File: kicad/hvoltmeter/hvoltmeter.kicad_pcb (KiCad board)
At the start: 2 copper layers, 14.4 x 24.9 mm, 34 parts, among them J1 USB_B_Micro-Connector, J2 SWC, J3 SWD, J4 Conn, J5 Conn, J6 Conn, SW1 SW_DPDT_x2, U1 LTC4054ES5-4.2, U2 AD8541, U3 MCP1700

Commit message: удалено:       STM32Cube/HV/.cproject 	удалено:       STM32Cube/HV/.mxproject 	удалено:       STM32Cube/HV/.project 	удалено:       STM32Cube/HV/.settings/language.settings.xml 	удалено:       STM32Cube/HV/.settings/stm32cubeide.project.prefs 	удалено:       STM32Cube/HV/Core/Inc/main.h 	удалено:       STM32Cube/HV/Core/Inc/stm32g0xx_hal_conf.h 	удалено:       STM32Cube/HV/Core/Inc/stm32g0xx_it.h 	удалено:       STM32Cube/HV/Core/Src/main.c 	удалено:       STM32Cube/HV/Core/Src/stm32g0xx_hal_msp.c 	удалено:       STM32Cube/HV/Core/Src/stm32g0xx_it.c 	удалено:       STM32Cube/HV/Core/Src/syscalls.c 	удалено:       STM32Cube/HV/Core/Src/sysmem.c 	удалено:       STM32Cube/HV/Core/Src/system_stm32g0xx.c 	удалено:       STM32Cube/HV/Core/Startup/startup_stm32g031f8px.s 	удалено:       STM32Cube/HV/Drivers/CMSIS/Device/ST/STM32G0xx/Include/stm32g031xx.h 	удалено:       STM32Cube/HV/Drivers/CMSIS/Device/ST/STM32G0xx/Include/stm32g0xx.h 	удалено:       STM32Cube/HV/Drivers/CMSIS/Device/ST/STM32G0xx/Include/system_stm32g0xx.h 	удалено:       STM32Cube/HV/Drivers/CMSIS/Include/cmsis_armcc.h 	удалено:       STM32Cube/HV/Drivers/CMSIS/Include/cmsis_armclang.h 	удалено:       STM32Cube/HV/Drivers/CMSIS/Include/cmsis_armclang_ltm.h 	удалено:       STM32Cube/HV/Drivers/CMSIS/Include/cmsis_compiler.h 	удалено:       STM32Cube/HV/Drivers/CMSIS/Include/cmsis_gcc.h 	удалено:       STM32Cube/HV/Drivers/CMSIS/Include/cmsis_iccarm.h 	удалено:       STM32Cube/HV/Drivers/CMSIS/Include/cmsis_version.h 	удалено:       STM32Cube/HV/Drivers/CMSIS/Include/core_armv81mml.h 	удалено:       STM32Cube/HV/Drivers/CMSIS/Include/core_armv8mbl.h 	удалено:       STM32Cube/HV/Drivers/CMSIS/Include/core_armv8mml.h 	удалено:       STM32Cube/HV/Drivers/CMSIS/Include/core_cm0.h 	удалено:       STM32Cube/HV/Drivers/CMSIS/Include/core_cm0plus.h 	удалено:       STM32Cube/HV/Drivers/CMSIS/Include/core_cm1.h 	удалено:       STM32Cube/HV/Drivers/CMSIS/Include/core_cm23.h 	удалено:       STM32Cube/HV/Drivers/CMSIS/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
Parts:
- R6: value 10G -> 5G
- R8: value 4.7k -> 10k
- moved C11 30.4 mm to (38.5, 63.5)
- moved C12 27.9 mm to (40.6, 63.5)
- moved C9 26.3 mm to (41.7, 63.5), turned to 270 degrees
- moved R3 26.3 mm to (47.5, 68.8), turned to 90 degrees
- moved R4 25.8 mm to (39.5, 66.3)
- moved C1 25.5 mm to (40.0, 75.4)
- moved C2 25.5 mm to (42.2, 68.2)
- moved C5 25.5 mm to (47.7, 65.2)
- moved R5 25.5 mm to (48.0, 76.4)
- moved C3 25.5 mm to (40.1, 61.5)
- moved C4 25.5 mm to (46.7, 73.2)
- moved C6 25.5 mm to (47.5, 68.8)
- moved C7 25.5 mm to (46.7, 76.5)
- moved D1 25.5 mm to (41.6, 62.5)
- moved J4 25.5 mm to (38.2, 59.8)
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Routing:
- net Net-(D2-Pad15): track 2.99 -> 10.7 mm
- net SDA: track 15.9 -> 9.25 mm
- net +BATT: track 21.7 -> 16.2 mm
- net Net-(D3-Pad12): track 1.84 -> 4.34 mm
- net SCL: track 7.03 -> 9.30 mm
- net GND: track 65.3 -> 66.8 mm
- net Net-(D3-Pad9): track 1.89 -> 3.32 mm
- net +2V8: track 42.3 -> 43.2 mm
- net Net-(D2-Pad18): track 4.77 -> 4.03 mm

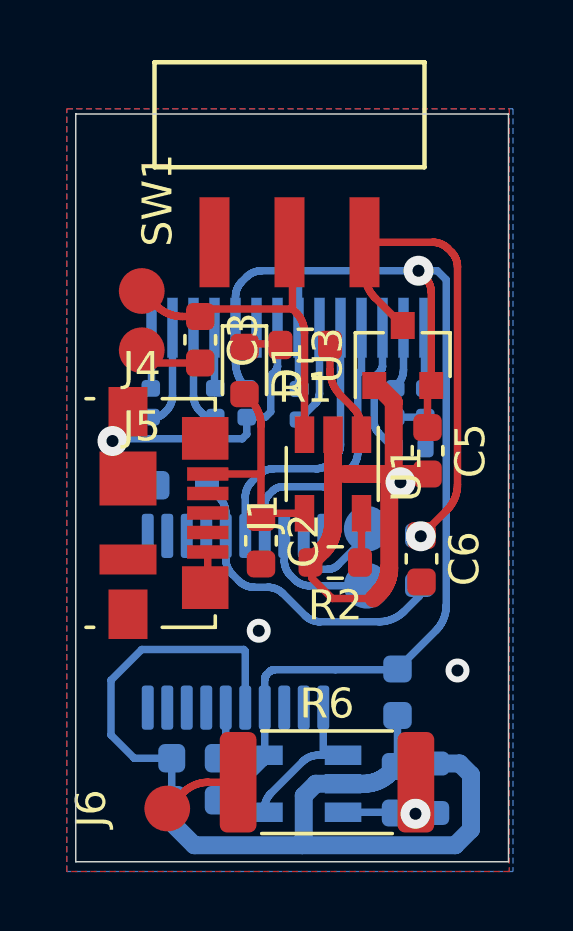
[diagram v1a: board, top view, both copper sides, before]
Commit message: изменено:      kicad/hvoltmeter/hvoltmeter.kicad_pcb 	изменено:      kicad/hvoltmeter/hvoltmeter.kicad_pcb-bak 	изменено:      kicad/hvoltmeter/hvoltmeter.sch 	изменено:      kicad/hvoltmeter/hvoltmeter.sch-bak
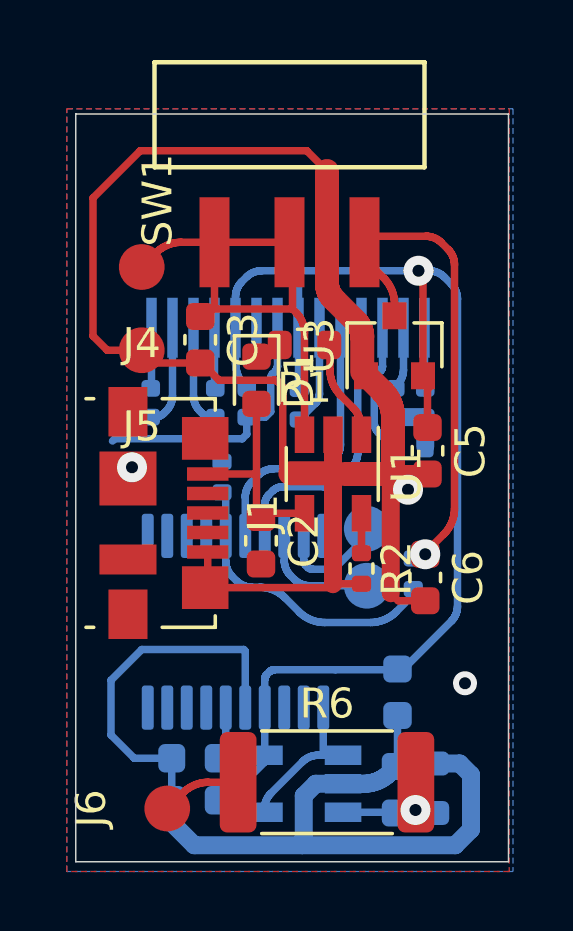
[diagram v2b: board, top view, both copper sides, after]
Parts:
- R2: footprint Resistor_SMD:R_0603_1608Metric -> Resistor_SMD:R_0402_1005Metric
- R3: value R -> 10k; footprint Resistor_SMD:R_0603_1608Metric -> Resistor_SMD:R_0402_1005Metric
- R4: value R -> 20k; footprint Resistor_SMD:R_0603_1608Metric -> Resistor_SMD:R_0402_1005Metric
- moved R4 1.35 mm to (40.9, 66.0), turned to 90 degrees
- moved R2 0.90 mm to (45.5, 69.1), turned to 270 degrees
- moved J4 0.80 mm to (38.2, 59.0)
- moved C6 0.64 mm to (47.6, 69.4)
- moved D1 0.52 mm to (42.0, 62.8)
- moved R3 0.49 mm to (47.2, 69.2)
- moved U3 0.43 mm to (46.6, 61.6)
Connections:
- SW1 pad 3: (no net) -> Net-(C3-Pad1)
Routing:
- net GND: track 66.8 -> 100.8 mm, vias 4 -> 3
- net Net-(C3-Pad1): track 12.0 -> 17.2 mm
- net Net-(D2-Pad15): track 10.7 -> 9.97 mm
- net Net-(C2-Pad1): track 7.58 -> 6.98 mm

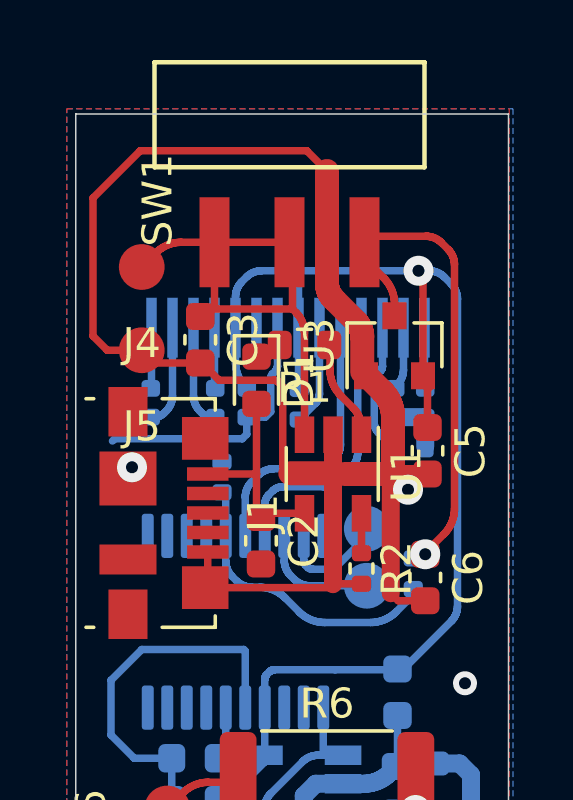
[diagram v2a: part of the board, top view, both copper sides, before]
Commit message: изменено:      kicad/hvoltmeter/hvoltmeter.kicad_pcb 	изменено:      kicad/hvoltmeter/hvoltmeter.kicad_pcb-bak 	изменено:      kicad/hvoltmeter/hvoltmeter.sch 	изменено:      kicad/hvoltmeter/hvoltmeter.sch-bak
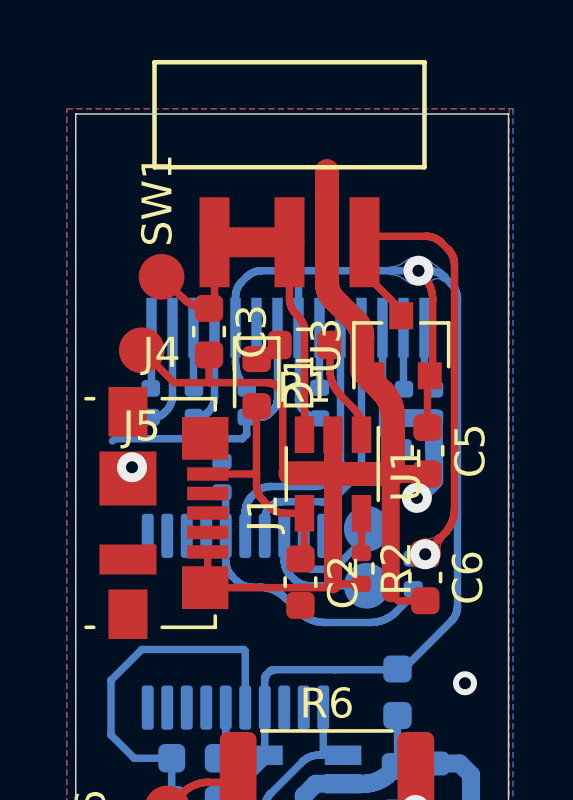
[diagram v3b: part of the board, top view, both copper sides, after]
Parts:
- moved C2 1.91 mm to (43.5, 69.5)
- moved J4 0.74 mm to (38.9, 59.4)
- moved C12 0.71 mm to (39.9, 63.5), turned to 270 degrees
- moved R8 0.68 mm to (44.1, 63.6), turned to 270 degrees
- moved C3 0.40 mm to (40.4, 61.2)
- moved C10 0.29 mm to (46.9, 63.6)
- moved C13 0.29 mm to (47.9, 63.6)
- moved R7 0.29 mm to (47.4, 65.1)
- moved U3 0.23 mm to (46.9, 61.6)
- moved D1 0.08 mm to (42.0, 62.9)
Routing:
- net GND: track 100.8 -> 88.3 mm
- net Net-(C3-Pad1): track 17.2 -> 13.3 mm
- net +2V8: track 43.2 -> 45.0 mm
- net Net-(C12-Pad1): track 3.41 -> 2.03 mm
- net Net-(C12-Pad2): track 2.03 -> 3.39 mm
- net Net-(D3-Pad9): track 3.32 -> 2.00 mm
- net Net-(C2-Pad1): track 6.98 -> 8.01 mm

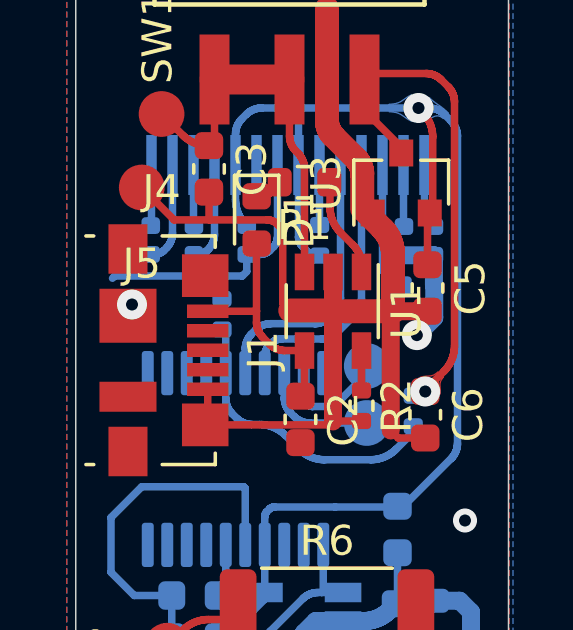
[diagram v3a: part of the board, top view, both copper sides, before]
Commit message: изменено:      kicad/hvoltmeter/hvoltmeter.kicad_pcb 	изменено:      kicad/hvoltmeter/hvoltmeter.kicad_pcb-bak 	изменено:      kicad/hvoltmeter/hvoltmeter.sch 	изменено:      kicad/hvoltmeter/hvoltmeter.sch-bak
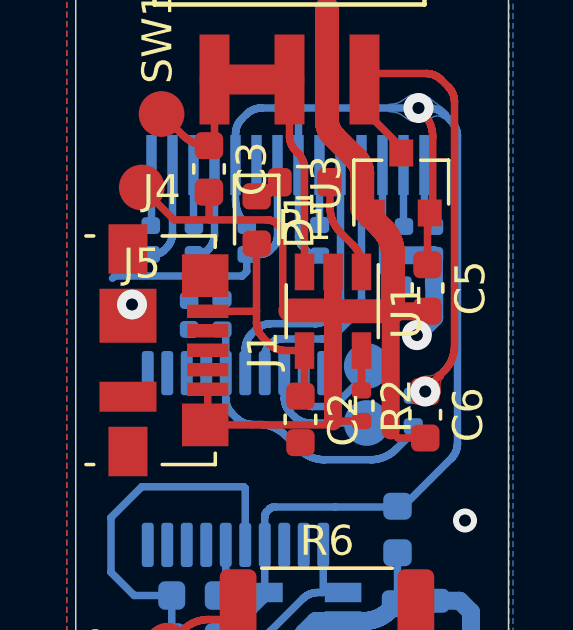
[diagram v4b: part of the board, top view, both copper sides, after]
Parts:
- added C14: 2.2uF, Capacitor_SMD:C_0402_1005Metric, B.Cu at (39.8, 66.0)
- R5: value 10M -> 4.7M
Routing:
- net Net-(C14-Pad2): track 9.97 -> 11.1 mm

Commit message: изменено:      kicad/hvoltmeter/hvoltmeter.kicad_pcb 	изменено:      kicad/hvoltmeter/hvoltmeter.kicad_pcb-bak
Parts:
- moved C1 11.0 mm to (42.3, 64.6)
- moved R5 11.0 mm to (50.3, 65.6)
- moved C2 11.0 mm to (45.8, 58.7)
- moved C4 11.0 mm to (49.0, 62.4)
- moved C5 11.0 mm to (50.0, 54.4)
- moved D1 11.0 mm to (44.3, 52.1)
- moved J3 11.0 mm to (48.0, 58.9)
- moved J4 11.0 mm to (41.2, 48.5)
- moved R2 11.0 mm to (47.8, 58.3)
- moved R4 11.0 mm to (43.2, 55.2)
- moved R8 11.0 mm to (46.4, 52.8)
- moved SW1 11.0 mm to (45.4, 45.9)
- moved C10 11.0 mm to (49.2, 52.8)
- moved C11 11.0 mm to (40.8, 52.8)
- moved C12 11.0 mm to (42.2, 52.8)
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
